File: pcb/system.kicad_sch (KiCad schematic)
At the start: 3 parts, among them J1 USB_C_Receptacle, U1 RP2040, U2 W25Q128JVS

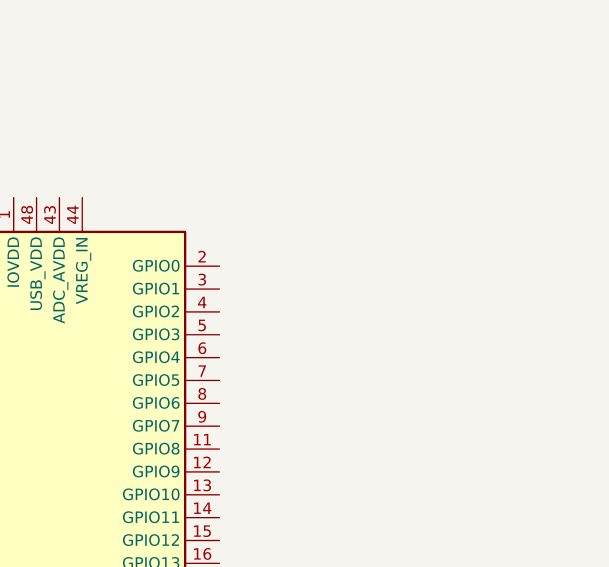
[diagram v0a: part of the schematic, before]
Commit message: feat: BME280 sensor
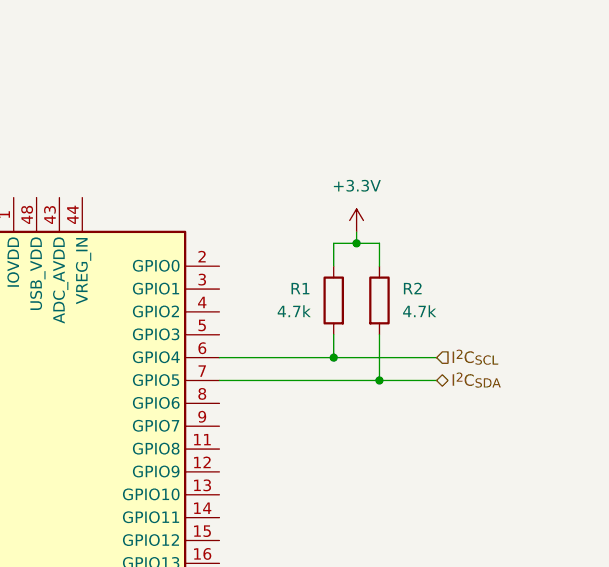
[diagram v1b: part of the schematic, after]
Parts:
- added R1, R2: 4.7k, symbol Device:R
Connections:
- net I^{2}C_{SCL}: now reaches U1.6 (GPIO4)
- net I^{2}C_{SCL}: now also R1.2
- net I^{2}C_{SDA}: now reaches U1.7 (GPIO5)
- net I^{2}C_{SDA}: now also R2.2
- new net +3.3V: R1.1, R2.1

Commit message: chore: docs
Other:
- company: (none) -> Ivan Leonard O Aparte <ivanleonard.aparte@cit.edu>
- title: (none) -> Banshee Microcontroller + Supporting Systems
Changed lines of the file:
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@@
 	(generator_version "9.0")
 	(paper "A4")
+	(title_block
+		(title "Banshee Microcontroller + Supporting Systems")
+		(date "2026-01-29")
+		(rev "1")
+		(company "Ivan Leonard O Aparte <ivanleonard.aparte@cit.edu>")
+	)
 	(junction
 		(at 200.66 68.58)

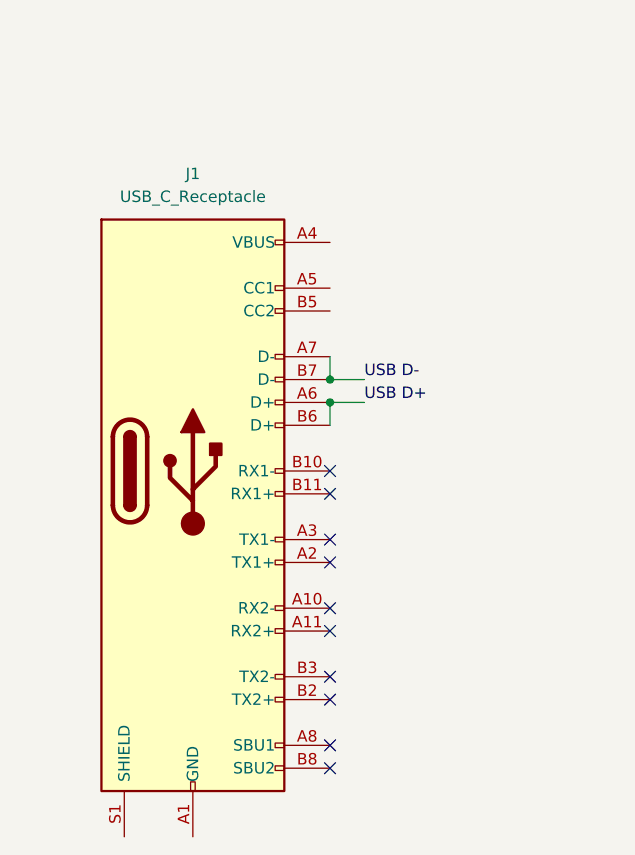
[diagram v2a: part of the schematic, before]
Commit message: chore: used simpler USB-C receptacle
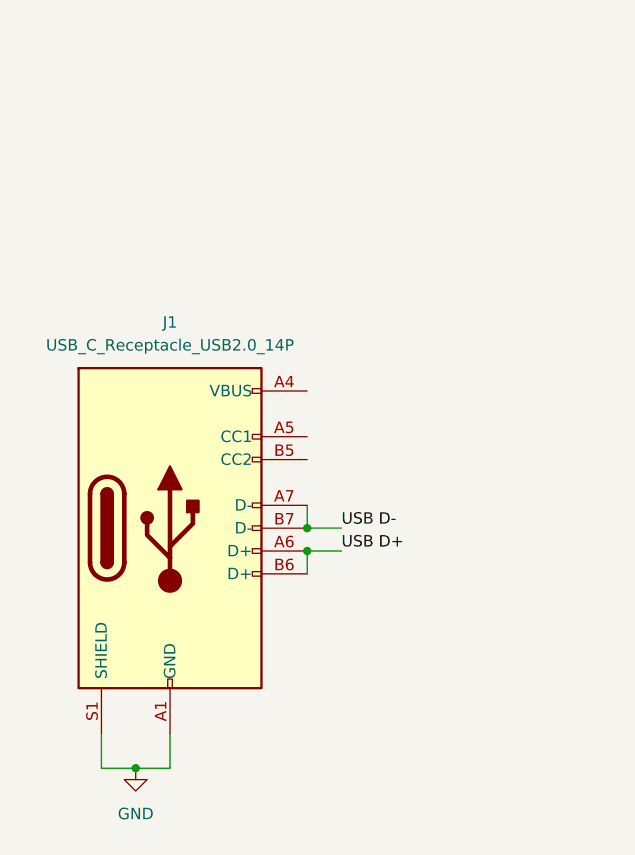
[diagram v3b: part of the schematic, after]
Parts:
- removed J1: USB_C_Receptacle, symbol Connector:USB_C_Receptacle
- added J1: USB_C_Receptacle_USB2.0_14P, symbol Connector:USB_C_Receptacle_USB2.0_14P
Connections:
- net USB D+: now also J1.A6 (D+), J1.B6 (D+)
- net USB D-: now also J1.A7 (D-), J1.B7 (D-)
- new net: J1.A4 (VBUS), J1.A9 (VBUS), J1.B4 (VBUS), J1.B9 (VBUS)
- new net GND: J1.A1 (GND), J1.A12 (GND), J1.B1 (GND), J1.B12 (GND), J1.S1 (SHIELD)
- no-connect marks 10 -> 0
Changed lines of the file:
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@@
 	)
 	(junction
-		(at 57.15 142.24)
+		(at 35.56 182.88)
+		(diameter 0)
+		(color 0 0 0 0)
+	)
+	(junction
+		(at 54.61 156.21)
+		(diameter 0)
+		(color 0 0 0 0)
+	)
+	(junction
+		(at 54.61 158.75)
 		(diameter 0)
 		(color 0 0 0 0)
@@
 		(color 0 0 0 0)
 	)
-	(junction
-		(at 57.15 139.7)
-		(diameter 0)
-		(color 0 0 0 0)
-	)
-	(no_connect
-		(at 57.15 165.1)
-	)
-	(no_connect
-		(at 57.15 157.48)
-	)
-	(no_connect
-		(at 57.15 149.86)
-	)
-	(no_connect
-		(at 57.15 180.34)
-	)
-	(no_connect
-		(at 57.15 172.72)
-	)
-	(no_connect
-		(at 57.15 152.4)
-	)
-	(no_connect
-		(at 57.15 182.88)
-	)
-	(no_connect
-		(at 57.15 175.26)
-	)
-	(no_connect
-		(at 57.15 160.02)
-	)
-	(no_connect
-		(at 57.15 167.64)
-	)
 	(wire
 		(pts
@@
 	(wire
 		(pts
+			(xy 31.75 179.07) (xy 31.75 182.88)
+		)
+		(stroke
+			(width 0)
+			(type default)
+		)
+	)
+	(wire
+		(pts
 			(xy 133.35 83.82) (xy 137.16 83.82)
 		)
@@
 	(wire
 		(pts
+			(xy 31.75 182.88) (xy 35.56 182.88)
+		)
+		(stroke
+			(width 0)
+			(type default)
+		)
+	)
+	(wire
+		(pts
 			(xy 63.5 41.91) (xy 67.31 41.91)
 		)
@@
 	(wire
 		(pts
-			(xy 57.15 142.24) (xy 60.96 142.24)
+			(xy 54.61 158.75) (xy 58.42 158.75)
 		)
 		(stroke
@@
 	(wire
 		(pts
-			(xy 57.15 137.16) (xy 57.15 139.7)
+			(xy 54.61 153.67) (xy 54.61 156.21)
 		)
 		(stroke
@@
 	(wire
 		(pts
-			(xy 57.15 139.7) (xy 60.96 139.7)
+			(xy 54.61 156.21) (xy 58.42 156.21)
 		)
 		(stroke
@@
 	(wire
 		(pts
+			(xy 35.56 182.88) (xy 39.37 182.88)
+		)
+		(stroke
+			(width 0)
+			(type default)
+		)
+	)
+	(wire
+		(pts
 			(xy 203.2 55.88) (xy 205.74 55.88)
 		)
@@
 	(wire
 		(pts
-			(xy 57.15 142.24) (xy 57.15 144.78)
+			(xy 54.61 158.75) (xy 54.61 161.29)
+		)
+		(stroke
+			(width 0)
+			(type default)
+		)
+	)
+	(wire
+		(pts
+			(xy 39.37 182.88) (xy 39.37 179.07)
 		)
 		(stroke
@@
 	)
 	(label "USB D+"
-		(at 60.96 142.24 0)
+		(at 58.42 158.75 0)
 		(effects
 			(font
@@
 	)
 	(label "USB D-"
-		(at 60.96 139.7 0)
+		(at 58.42 156.21 0)
 		(effects
 			(font
@@
 				(path "/9bba97c2-2e09-46fb-bf2a-7de104403c7c/a98a71c0-d58c-4841-9b05-a84df7de5fc9"
 					(reference "U1")
-					(unit 1)
-				)
-			)
-		)
-	)
-	(symbol
-		(lib_id "Connector:USB_C_Receptacle")
-		(at 41.91 149.86 0)
-		(unit 1)
-		(exclude_from_sim no)
-		(in_bom yes)
-		(on_board yes)
-		(dnp no)
-		(fields_autoplaced yes)
-		(property "Reference" "J1"
-			(at 41.91 116.84 0)
-			(effects
-				(font
-					(size 1.27 1.27)
-				)
-			)
-		)
-		(property "Value" "USB_C_Receptacle"
-			(at 41.91 119.38 0)
-			(effects
-				(font
-					(size 1.27 1.27)
-				)
-			)
-		)
-		(property "Footprint" ""
-			(at 45.72 149.86 0)
-			(effects
-				(font
-					(size 1.27 1.27)
-				)
-				(hide yes)
-			)
-		)
-		(property "Datasheet" "https://www.usb.org/sites/default/files/documents/usb_type-c.zip"
-			(at 45.72 149.86 0)
-			(effects
-				(font
-					(size 1.27 1.27)
-				)
-				(hide yes)
-			)
-		)
-		(property "Description" "USB Full-Featured Type-C Receptacle connector"
-			(at 41.91 149.86 0)
-			(effects
-				(font
-					(size 1.27 1.27)
-				)
-				(hide yes)
-			)
-		)
-		(pin "A12"
-		)
-		(pin "A1"
-		)
-		(pin "B4"
-		)
-		(pin "A2"
-		)
-		(pin "A5"
-		)
-		(pin "A6"
-		)
-		(pin "B9"
-		)
-		(pin "B5"
-		)
-		(pin "B11"
-		)
-		(pin "B8"
-		)
-		(pin "A3"
-		)
-		(pin "B7"
-		)
-		(pin "B6"
-		)
-		(pin "B10"
-		)
-		(pin "A8"
-		)
-		(pin "A4"
-		)
-		(pin "A9"
-		)
-		(pin "B2"
-		)
-		(pin "S1"
-		)
-		(pin "A11"
-		)
-		(pin "B1"
-		)
-		(pin "B3"
-		)
-		(pin "A7"
-		)
-		(pin "B12"
-		)
-		(pin "A10"
-		)
-		(instances
-			(project ""
-				(path "/9bba97c2-2e09-46fb-bf2a-7de104403c7c/a98a71c0-d58c-4841-9b05-a84df7de5fc9"
-					(reference "J1")
 					(unit 1)
 				)
@@
 					(unit 1)
 				)
+			)
+		)
+	)
+	(symbol
+		(lib_id "Connector:USB_C_Receptacle_USB2.0_14P")
+		(at 39.37 156.21 0)
+		(unit 1)
+		(exclude_from_sim no)
+		(in_bom yes)
+		(on_board yes)
+		(dnp no)
+		(fields_autoplaced yes)
+		(property "Reference" "J1"
+			(at 39.37 133.35 0)
+			(effects
+				(font
+					(size 1.27 1.27)
+				)
+			)
+		)
+		(property "Value" "USB_C_Receptacle_USB2.0_14P"
+			(at 39.37 135.89 0)
+			(effects
+				(font
+					(size 1.27 1.27)
+				)
+			)
+		)
+		(property "Footprint" ""
+			(at 43.18 156.21 0)
+			(effects
+				(font
+					(size 1.27 1.27)
+				)
+				(hide yes)
+			)
+		)
+		(property "Datasheet" "https://www.usb.org/sites/default/files/documents/usb_type-c.zip"
+			(at 43.18 156.21 0)
+			(effects
+				(font
+					(size 1.27 1.27)
+				)
+				(hide yes)
+			)
+		)
+		(property "Description" "USB 2.0-only 14P Type-C Receptacle connector"
+			(at 39.37 156.21 0)
+			(effects
+				(font
+					(size 1.27 1.27)
+				)
+				(hide yes)
+			)
+		)
+		(pin "B7"
+		)
+		(pin "A9"
+		)
+		(pin "A4"
+		)
+		(pin "A7"
+		)
+		(pin "B6"
+		)
+		(pin "A5"
+		)
+		(pin "S1"
+		)
+		(pin "B5"
+		)
+		(pin "A6"
+		)
+		(pin "B9"
+		)
+		(pin "B12"
+		)
+		(pin "B4"
+		)
+		(pin "A1"
+		)
+		(pin "A12"
+		)
+		(pin "B1"
+		)
+		(instances
+			(project ""
+				(path "/9bba97c2-2e09-46fb-bf2a-7de104403c7c/a98a71c0-d58c-4841-9b05-a84df7de5fc9"
+					(reference "J1")
+					(unit 1)
+				)
+			)
+		)
+	)
+	(symbol
+		(lib_id "power:GND")
+		(at 35.56 182.88 0)
+		(unit 1)
+		(exclude_from_sim no)
+		(in_bom yes)
+		(on_board yes)
+		(dnp no)
+		(fields_autoplaced yes)
+		(property "Reference" "#PWR08"
+			(at 35.56 189.23 0)
+			(effects
+				(font
+					(size 1.27 1.27)
+				)
+				(hide yes)
+			)
+		)
+		(property "Value" "GND"
+			(at 35.56 187.96 0)
+			(effects
+				(font
+					(size 1.27 1.27)
+				)
+			)
+		)
+		(property "Footprint" ""
+			(at 35.56 182.88 0)
+			(effects
+				(font
+					(size 1.27 1.27)
+				)
+				(hide yes)
+			)
+		)
+		(property "Datasheet" ""
+			(at 35.56 182.88 0)
+			(effects
+				(font
+					(size 1.27 1.27)
+				)
+				(hide yes)
+			)
+		)
+		(property "Description" "Power symbol creates a global label with name \"GND\" , ground"
+			(at 35.56 182.88 0)
+			(effects
+				(font
+					(size 1.27 1.27)
+				)
+				(hide yes)
+			)
+		)
+		(pin "1"
+		)
+		(instances
+			(project ""
+				(path "/9bba97c2-2e09-46fb-bf2a-7de104403c7c/a98a71c0-d58c-4841-9b05-a84df7de5fc9"
+					(reference "#PWR08")
+					(unit 1)
+				)

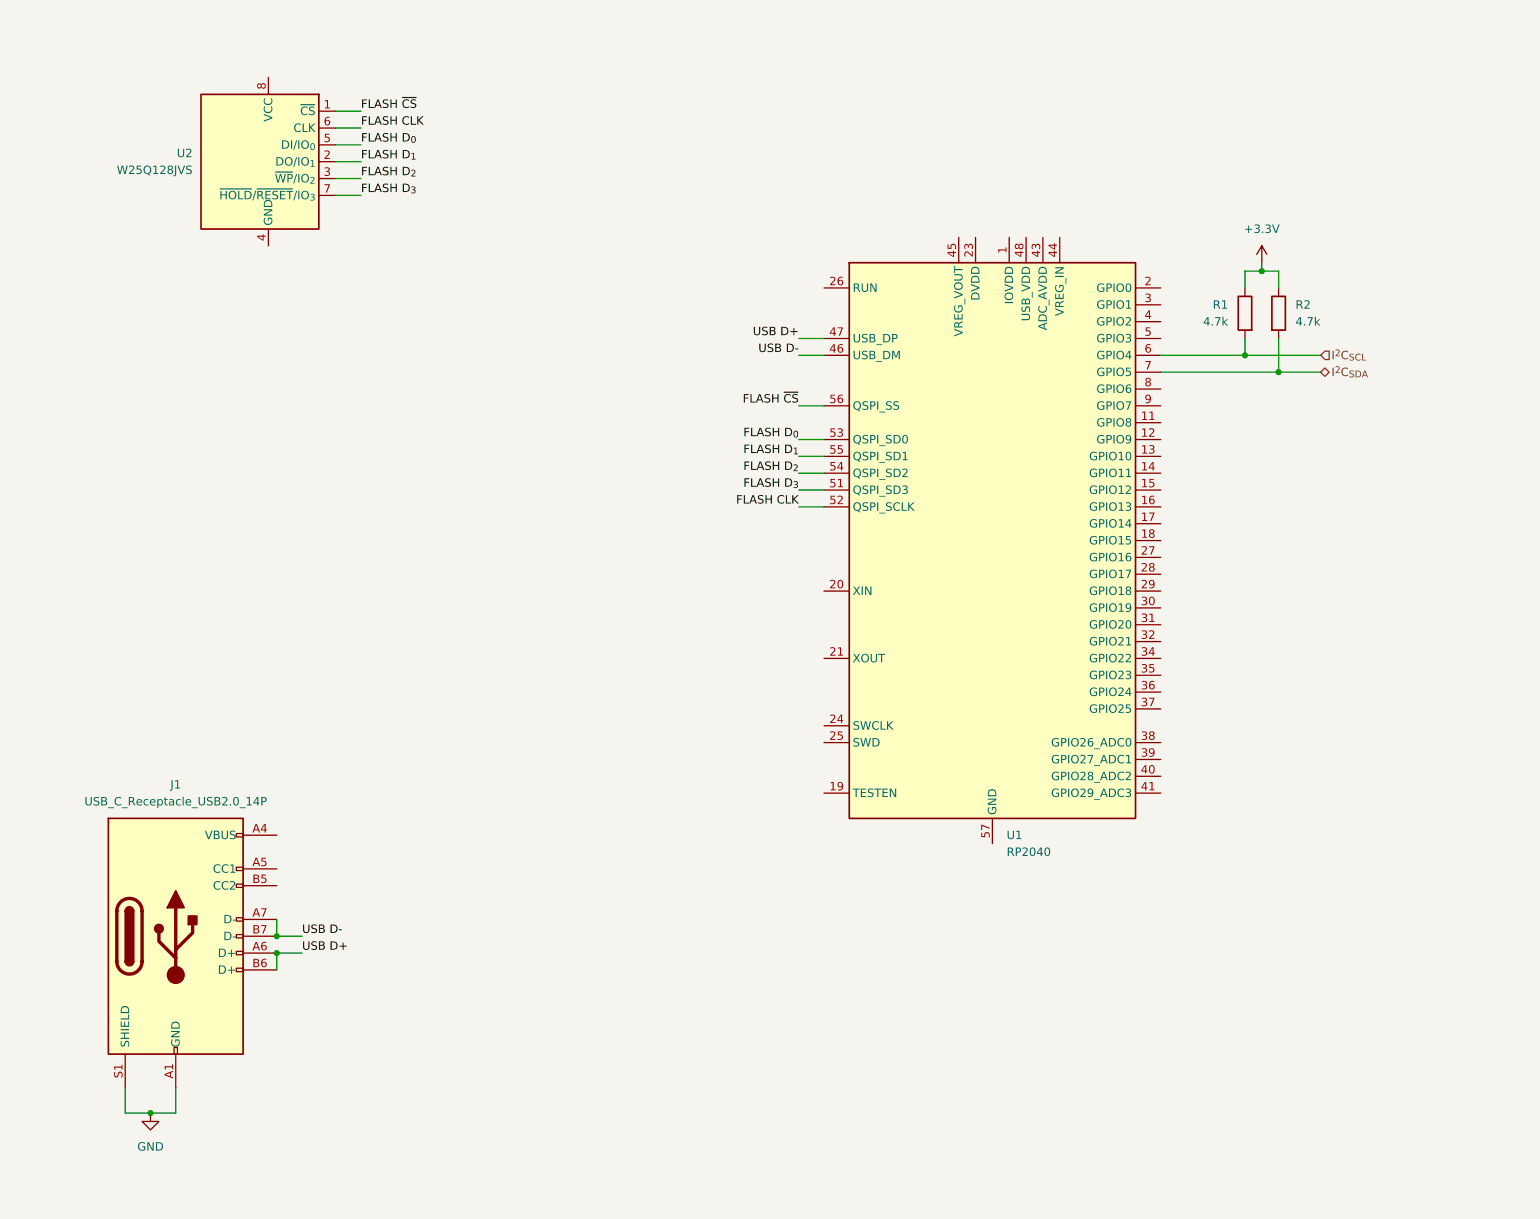
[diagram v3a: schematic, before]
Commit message: feat: Flash and FRAM
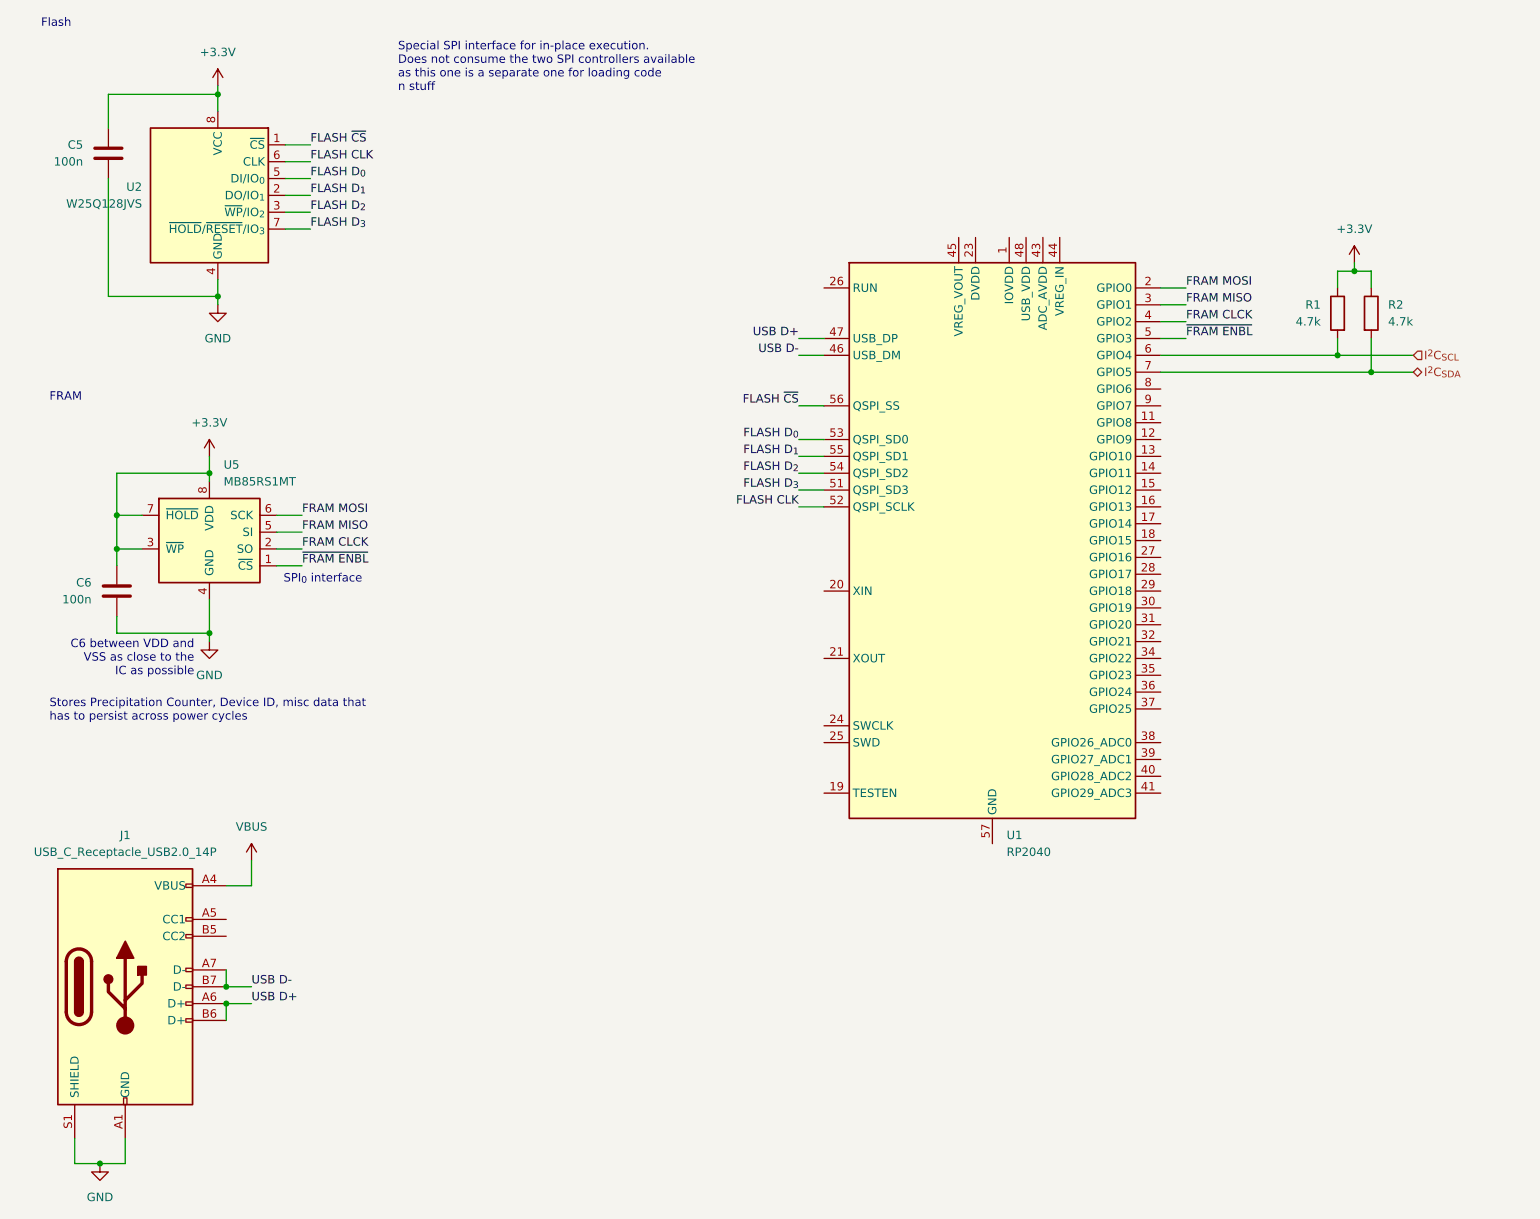
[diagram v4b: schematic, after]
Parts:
- added C5, C6: 100n, symbol Device:C
- added U5: MB85RS1MT, symbol Memory_NVRAM:MB85RS1MT
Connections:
- net +3.3V: now also U2.8 (VCC), C5.1, C6.1, U5.3 (~{WP}), U5.7 (~{HOLD}), U5.8 (VDD)
- net GND: now also U2.4 (GND), C5.2, C6.2, U5.4 (GND)
- net FRAM MOSI: now reaches U1.2 (GPIO0)
- net FRAM MOSI: now also U5.6 (SCK)
- net FRAM MISO: now reaches U1.3 (GPIO1)
- net FRAM MISO: now also U5.5 (SI)
- net FRAM CLCK: now reaches U1.4 (GPIO2)
- net FRAM CLCK: now also U5.2 (SO)
- net ~{FRAM ENBL}: now reaches U1.5 (GPIO3)
- net ~{FRAM ENBL}: now also U5.1 (~{CS})
- net VBUS: now reaches J1.A4 (VBUS), J1.A9 (VBUS), J1.B4 (VBUS), J1.B9 (VBUS)
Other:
- note added: "C6 between VDD and VSS as close to the IC as possible"
- note added: "FRAM"
- note added: "Flash"
- note added: "SPI_{0} interface"
- note added: "Special SPI interface for in-place execution. Does not consume the two SPI controllers available as this one is a separate one for loading code n stuff"
- note added: "Stores Precipitation Counter, Device ID, misc data that has to persist across power cycles"
- moved on the sheet: J1, R1, R2, U2

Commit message: feat: RJ11 connector, partial BOM fulfillment
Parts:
- U1: JLCPCB Part# (none) -> C2040
- U2: JLCPCB Part# (none) -> C97521
- U5: footprint (none) -> Package_SO:SSOP-8_3.9x5.05mm_P1.27mm; JLCPCB Part# (none) -> C126733
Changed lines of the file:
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@@
+			)
+		)
+		(property "JLCPCB Part#" ""
+			(at 30.48 104.14 0)
+			(effects
+				(font
+					(size 1.27 1.27)
+				)
+				(hide yes)
 			)
 		)
@@
 			)
 		)
+		(property "JLCPCB Part#" "C2040"
+			(at 162.56 96.52 0)
+			(effects
+				(font
+					(size 1.27 1.27)
+				)
+				(hide yes)
+			)
+		)
 		(pin "1"
 		)
@@
 			)
 		)
-		(property "Footprint" ""
+		(property "Footprint" "Package_SO:SSOP-8_3.9x5.05mm_P1.27mm"
 			(at 35.56 96.52 0)
 			(effects
@@
 			)
 		)
+		(property "JLCPCB Part#" "C126733"
+			(at 44.45 95.25 0)
+			(effects
+				(font
+					(size 1.27 1.27)
+				)
+				(hide yes)
+			)
+		)
 		(pin "1"
 		)
@@
 		)
 		(property "Description" "Unpolarized capacitor"
+			(at 29.21 38.1 0)
+			(effects
+				(font
+					(size 1.27 1.27)
+				)
+				(hide yes)
+			)
+		)
+		(property "JLCPCB Part#" ""
 			(at 29.21 38.1 0)
 			(effects
@@
 			)
 		)
+		(property "JLCPCB Part#" ""
+			(at 214.63 62.23 0)
+			(effects
+				(font
+					(size 1.27 1.27)
+				)
+				(hide yes)
+			)
+		)
 		(pin "2"
 		)
@@
 			)
 		)
+		(property "JLCPCB Part#" "C97521"
+			(at 45.72 44.45 0)
+			(effects
+				(font
+					(size 1.27 1.27)
+				)
+				(hide yes)
+			)
+		)
 		(pin "8"
 		)
@@
 			)
 		)
+		(property "JLCPCB Part#" ""
+			(at 219.71 62.23 0)
+			(effects
+				(font
+					(size 1.27 1.27)
+				)
+				(hide yes)
+			)
+		)
 		(pin "2"
 		)
@@
 			(at 31.75 163.83 0)
 			(effects
+				(font
+					(size 1.27 1.27)
+				)
+				(hide yes)
+			)
+		)
+		(property "JLCPCB Part#" ""
+			(at 31.75 163.83 0)
+			(effects
